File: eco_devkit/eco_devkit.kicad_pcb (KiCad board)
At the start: 2 copper layers, 98.5 x 78 mm, 144 parts, among them J1 USB_C_Receptacle_USB2.0_16P, J10 Micro_SD_Card_Det1, J11 DISPLAY FFC, J2 Conn_02x20_Counter_Clockwise, J3 ADC_SEL1, J4 BluetoothHeader, J5 ADC_SEL1, J6 ADC_SEL1, J7 ADC_SEL1, J8 USB_C_Receptacle_USB2.0_16P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

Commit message: chore: routing some PCB components
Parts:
- moved R34 2.35 mm to (179.1, 44.4), turned to 90 degrees
- moved C25 1.04 mm to (177.9, 44.3), turned to -90 degrees
- moved C41 0.95 mm to (215.6, 54.0), turned to 90 degrees
- moved R42 0.20 mm to (213.3, 54.0)
- turned R43 to 90 degrees
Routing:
- net DISPLAY_SCK: track 0.00 -> 84.8 mm, vias 0 -> 2
- net DISPLAY_MOSI: track 0.00 -> 84.0 mm, vias 0 -> 2
- net GPIO21: track 0.00 -> 40.2 mm
- net ACCEL_SCK: track 22.4 -> 60.1 mm, vias 0 -> 2
- net GPIO22: track 0.00 -> 36.6 mm, vias 0 -> 2
- net ACCEL_INT1: track 3.79 -> 38.7 mm, vias 0 -> 2
- net ACCEL_MOSI: track 22.3 -> 56.8 mm, vias 0 -> 2
- net ACCEL_INT2: track 3.79 -> 38.2 mm, vias 0 -> 2
- net PIN_LIGHT_SENS_SCL: track 0.00 -> 34.1 mm, vias 0 -> 2
- net PIN_LIGHT_SENS_SDA: track 0.00 -> 33.3 mm, vias 0 -> 2
- net ACCEL_MISO: track 21.7 -> 48.8 mm, vias 0 -> 2
- net Net-(R7-Pad2): track 0.00 -> 24.9 mm
- net +VDISP: track 5.67 -> 19.4 mm
- net +3V3: track 111.0 -> 112.7 mm

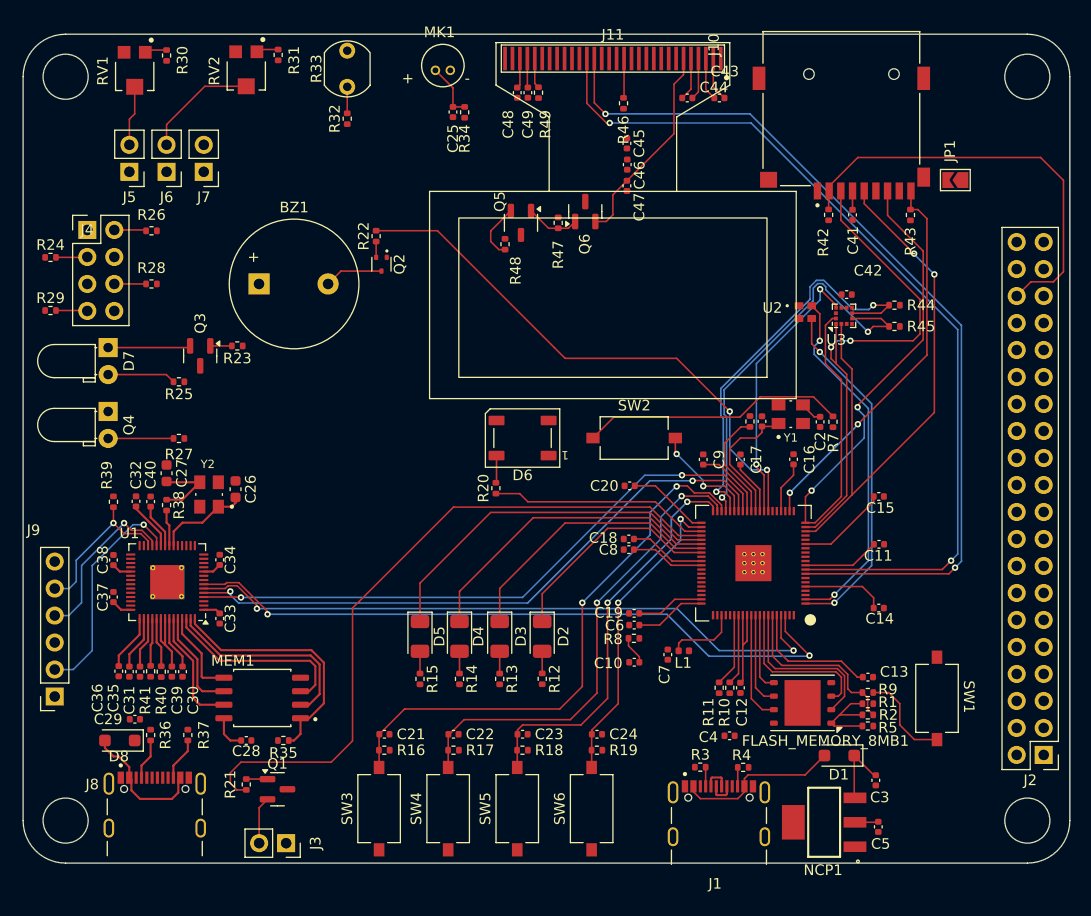
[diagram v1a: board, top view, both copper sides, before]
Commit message: routed all components except header and copper pours
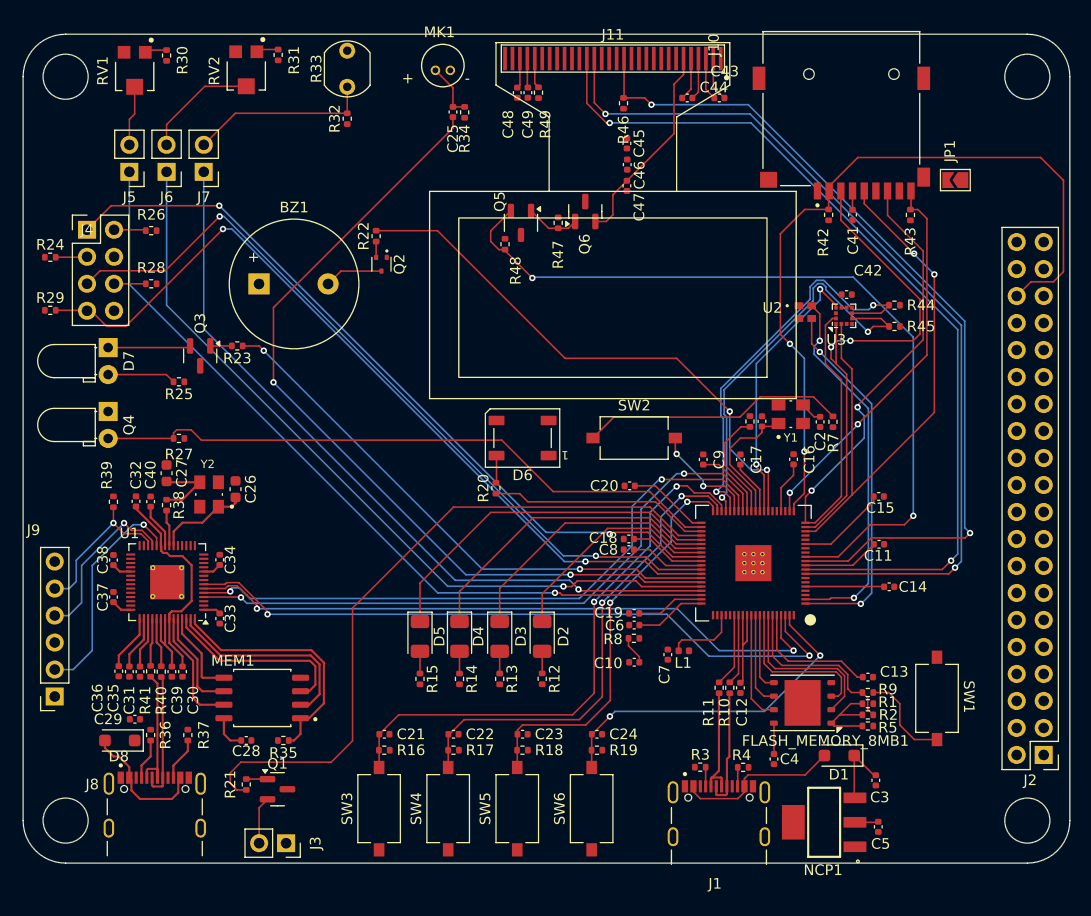
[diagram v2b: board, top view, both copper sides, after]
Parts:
- moved C4 4.72 mm to (208.2, 105.2), turned to -90 degrees
- moved C14 2.23 mm to (219.0, 89.0)
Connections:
- C30 pad 1: +1V1 -> +1V1_PROBRE
- C31 pad 1: +1V1 -> +1V1_PROBRE
- C32 pad 2: +1V1 -> +1V1_PROBRE
- J2 pad 11: PIN_WIFI_RESET_BL -> GPIO42_ADC2
- J2 pad 12: PIN_WIFI_RX -> GPIO40_ADC0
- J2 pad 13: PIN_WIFI_TX -> GPIO41_ADC1
- J2 pad 28: GPIO43_ADC3 -> IR_TX
- J2 pad 29: GPIO42_ADC2 -> PIN_WIFI_RESET_BL
- J2 pad 30: GPIO41_ADC1 -> PIN_WIFI_TX
- J2 pad 31: GPIO40_ADC0 -> PIN_WIFI_RX
- J2 pad 6: /MCU/GPIO2 -> PIN_BTN4
- RP2350B1 pad 4: PIN_WIFI_RESET_BL -> GPIO42_ADC2
- RP2350B1 pad 42: PIN_BTN4 -> IR_RX
- RP2350B1 pad 49: GPIO40_ADC0 -> PIN_WIFI_RX
- RP2350B1 pad 52: GPIO41_ADC1 -> PIN_WIFI_TX
- RP2350B1 pad 53: GPIO42_ADC2 -> PIN_WIFI_RESET_BL
- RP2350B1 pad 54: GPIO43_ADC3 -> IR_TX
- RP2350B1 pad 6: PIN_WIFI_RX -> GPIO40_ADC0
- RP2350B1 pad 7: PIN_WIFI_TX -> GPIO41_ADC1
- RP2350B1 pad 79: /MCU/GPIO2 -> PIN_BTN4
- U1 pad 23: +1V1 -> +1V1_PROBRE
- U1 pad 45: +1V1 -> +1V1_PROBRE
- U1 pad 50: +1V1 -> +1V1_PROBRE
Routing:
- net GPIO44_ADC4: track 0.00 -> 80.0 mm, vias 0 -> 2
- net DISPLAY_RST: track 3.76 -> 81.4 mm, vias 0 -> 2
- net GPIO47_ADC7: track 0.00 -> 76.5 mm, vias 0 -> 1
- net PIN_WIFI_RESET_BL: track 2.97 -> 78.7 mm, vias 0 -> 2
- net GPIO45_ADC5: track 0.00 -> 74.3 mm, vias 0 -> 1
- net PIN_WIFI_TX: track 0.00 -> 74.2 mm, vias 0 -> 2
- net PIN_WIFI_RX: track 0.00 -> 72.7 mm, vias 0 -> 2
- net GPIO46_ADC6: track 0.00 -> 71.8 mm, vias 0 -> 1
- net DISPLAY_EN: track 5.35 -> 75.9 mm, vias 0 -> 2
- net IR_RX: track 6.16 -> 60.3 mm
- net IR_TX: track 0.00 -> 52.2 mm, vias 0 -> 2
- net GPIO21: track 40.2 -> 73.2 mm, vias 0 -> 2
- net +1V1_PROBRE: track 0.00 -> 24.8 mm
- net Net-(J7-Pin_2): track 2.49 -> 17.2 mm
- net +1V1: track 35.7 -> 21.2 mm
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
